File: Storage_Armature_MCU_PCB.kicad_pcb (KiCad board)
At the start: 4 copper layers, 163 x 152 mm, 221 parts, among them Q1 20N06, U10 NSI1200, U11 OPA333, U12 NSI1200, U13 OPA333, U14 USBLC6-2P6, U2 NSI1200, U23 RSCD06D3, U24 RSCD06D3, U25 RSCD06D3, U26 RSCD06D3, U3 NSI1200, U4 ADP3338AKCZ-3.3RL7, U5 ADP3338AKCZ-3.3RL7, U6 OPA333, U7 OPA333, U8 NSI1200, U9 OPA333

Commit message: VER1.0: добавил светодиоды, тестпоинты и мягкий старт 24В
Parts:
- added C100: 2.2u, Capacitor_SMD:C_0805_2012Metric_Pad1.18x1.45mm_HandSolder, B.Cu at (348.8, 111.8)
- added C101: 10n, Capacitor_SMD:C_0805_2012Metric_Pad1.18x1.45mm_HandSolder, B.Cu at (347.2, 115.2)
- added C102: 10n, Capacitor_SMD:C_0805_2012Metric_Pad1.18x1.45mm_HandSolder, B.Cu at (347.2, 108.0)
- added C103: 100n, Capacitor_SMD:C_0805_2012Metric_Pad1.18x1.45mm_HandSolder, B.Cu at (343.2, 111.8)
- added C104: 56p, Capacitor_SMD:C_0805_2012Metric_Pad1.18x1.45mm_HandSolder, B.Cu at (339.2, 111.8)
- added C72: 2.2u, Capacitor_SMD:C_0805_2012Metric_Pad1.18x1.45mm_HandSolder, B.Cu at (363.8, 157.8)
- added C75: 100n, Capacitor_SMD:C_0805_2012Metric_Pad1.18x1.45mm_HandSolder, B.Cu at (361.5, 157.8)
- added C76: 22n, Capacitor_SMD:C_0805_2012Metric_Pad1.18x1.45mm_HandSolder, F.Cu at (364.8, 157.8)
- added C77: 100n, Capacitor_SMD:C_0805_2012Metric_Pad1.18x1.45mm_HandSolder, B.Cu at (351.0, 157.8)
- added C78: 2.2u, Capacitor_SMD:C_0805_2012Metric_Pad1.18x1.45mm_HandSolder, B.Cu at (348.8, 157.8)
- added C79: 10n, Capacitor_SMD:C_0805_2012Metric_Pad1.18x1.45mm_HandSolder, B.Cu at (347.2, 161.2)
- added C80: 10n, Capacitor_SMD:C_0805_2012Metric_Pad1.18x1.45mm_HandSolder, B.Cu at (347.2, 154.0)
- added C81: 100n, Capacitor_SMD:C_0805_2012Metric_Pad1.18x1.45mm_HandSolder, B.Cu at (343.2, 157.8)
- added C86: 56p, Capacitor_SMD:C_0805_2012Metric_Pad1.18x1.45mm_HandSolder, B.Cu at (339.2, 157.8)
- added C87: 2.2u, Capacitor_SMD:C_0805_2012Metric_Pad1.18x1.45mm_HandSolder, B.Cu at (363.8, 134.8)
- added C88: 100n, Capacitor_SMD:C_0805_2012Metric_Pad1.18x1.45mm_HandSolder, B.Cu at (361.5, 134.8)
- added C89: 22n, Capacitor_SMD:C_0805_2012Metric_Pad1.18x1.45mm_HandSolder, F.Cu at (364.8, 134.8)
- added C90: 100n, Capacitor_SMD:C_0805_2012Metric_Pad1.18x1.45mm_HandSolder, B.Cu at (351.0, 134.8)
- added C91: 2.2u, Capacitor_SMD:C_0805_2012Metric_Pad1.18x1.45mm_HandSolder, B.Cu at (348.8, 134.8)
- added C92: 10n, Capacitor_SMD:C_0805_2012Metric_Pad1.18x1.45mm_HandSolder, B.Cu at (347.2, 138.2)
- added C93: 10n, Capacitor_SMD:C_0805_2012Metric_Pad1.18x1.45mm_HandSolder, B.Cu at (347.2, 131.0)
- added C94: 100n, Capacitor_SMD:C_0805_2012Metric_Pad1.18x1.45mm_HandSolder, B.Cu at (343.2, 134.8)
- added C95: 56p, Capacitor_SMD:C_0805_2012Metric_Pad1.18x1.45mm_HandSolder, B.Cu at (339.2, 134.8)
- added C96: 2.2u, Capacitor_SMD:C_0805_2012Metric_Pad1.18x1.45mm_HandSolder, B.Cu at (363.8, 111.8)
- added C97: 100n, Capacitor_SMD:C_0805_2012Metric_Pad1.18x1.45mm_HandSolder, B.Cu at (361.5, 111.8)
- added C98: 22n, Capacitor_SMD:C_0805_2012Metric_Pad1.18x1.45mm_HandSolder, F.Cu at (364.8, 111.8)
- added C99: 100n, Capacitor_SMD:C_0805_2012Metric_Pad1.18x1.45mm_HandSolder, B.Cu at (351.0, 111.8)
- added D13: ~, Package_TO_SOT_SMD:SOT-23, F.Cu at (339.1, 161.3)
- added D15: ~, Package_TO_SOT_SMD:SOT-23, F.Cu at (339.1, 138.3)
- added D16: ~, Package_TO_SOT_SMD:SOT-23, F.Cu at (339.1, 115.3)
- added D68: ~, LED_SMD:LED_0805_2012Metric, F.Cu at (237.8, 264.8)
- added D69: ~, LED_SMD:LED_0805_2012Metric, F.Cu at (262.8, 264.8)
- added D70: ~, LED_SMD:LED_0805_2012Metric, F.Cu at (287.8, 264.8)
- added D71: ~, LED_SMD:LED_0805_2012Metric, F.Cu at (312.8, 264.8)
- added J33: ~, Connector_Molex:Molex_Mini-Fit_Jr_5569-02A2_2x01_P4.20mm_Horizontal, F.Cu at (369.2, 149.2)
- added J36: ~, Connector_Molex:Molex_Mini-Fit_Jr_5569-02A2_2x01_P4.20mm_Horizontal, F.Cu at (369.2, 126.2)
- added J37: ~, Connector_Molex:Molex_Mini-Fit_Jr_5569-02A2_2x01_P4.20mm_Horizontal, F.Cu at (369.2, 103.2)
- added Q2: 20N06, Package_TO_SOT_SMD:TO-252-2, F.Cu at (230.2, 223.5)
- added R120: 1k, Resistor_SMD:R_0805_2012Metric_Pad1.20x1.40mm_HandSolder, F.Cu at (237.8, 267.5)
- added R121: 1k, Resistor_SMD:R_0805_2012Metric_Pad1.20x1.40mm_HandSolder, F.Cu at (262.8, 267.5)
- added R122: 1k, Resistor_SMD:R_0805_2012Metric_Pad1.20x1.40mm_HandSolder, F.Cu at (287.8, 267.5)
- added R123: 1k, Resistor_SMD:R_0805_2012Metric_Pad1.20x1.40mm_HandSolder, F.Cu at (312.8, 267.5)
- added R50: 10, Resistor_SMD:R_1206_3216Metric_Pad1.30x1.75mm_HandSolder, F.Cu at (370.8, 153.8)
- added R51: 100, Resistor_SMD:R_0805_2012Metric_Pad1.20x1.40mm_HandSolder, F.Cu at (368.0, 159.0)
- added R52: 100, Resistor_SMD:R_0805_2012Metric_Pad1.20x1.40mm_HandSolder, F.Cu at (368.0, 156.5)
- added R53: 10k, Resistor_SMD:R_0805_2012Metric_Pad1.20x1.40mm_HandSolder, F.Cu at (347.2, 159.0)
- added R56: 10k, Resistor_SMD:R_0805_2012Metric_Pad1.20x1.40mm_HandSolder, F.Cu at (347.2, 156.5)
- added R59: 20k, Resistor_SMD:R_0805_2012Metric_Pad1.20x1.40mm_HandSolder, F.Cu at (347.2, 161.2)
- added R60: 20k, Resistor_SMD:R_0805_2012Metric_Pad1.20x1.40mm_HandSolder, F.Cu at (347.2, 154.0)
- added R61: 120, Resistor_SMD:R_0805_2012Metric_Pad1.20x1.40mm_HandSolder, F.Cu at (339.2, 157.8)
- added R62: 10, Resistor_SMD:R_1206_3216Metric_Pad1.30x1.75mm_HandSolder, F.Cu at (370.8, 130.8)
- added R63: 100, Resistor_SMD:R_0805_2012Metric_Pad1.20x1.40mm_HandSolder, F.Cu at (368.0, 136.0)
- added R64: 100, Resistor_SMD:R_0805_2012Metric_Pad1.20x1.40mm_HandSolder, F.Cu at (368.0, 133.5)
- added R65: 10k, Resistor_SMD:R_0805_2012Metric_Pad1.20x1.40mm_HandSolder, F.Cu at (347.2, 136.0)
- added R66: 10k, Resistor_SMD:R_0805_2012Metric_Pad1.20x1.40mm_HandSolder, F.Cu at (347.2, 133.5)
- added R67: 20k, Resistor_SMD:R_0805_2012Metric_Pad1.20x1.40mm_HandSolder, F.Cu at (347.2, 138.2)
- added R68: 20k, Resistor_SMD:R_0805_2012Metric_Pad1.20x1.40mm_HandSolder, F.Cu at (347.2, 131.0)
- added R69: 120, Resistor_SMD:R_0805_2012Metric_Pad1.20x1.40mm_HandSolder, F.Cu at (339.2, 134.8)
- added R70: 10, Resistor_SMD:R_1206_3216Metric_Pad1.30x1.75mm_HandSolder, F.Cu at (370.8, 107.8)
- added R71: 100, Resistor_SMD:R_0805_2012Metric_Pad1.20x1.40mm_HandSolder, F.Cu at (368.0, 113.0)
- added R72: 100, Resistor_SMD:R_0805_2012Metric_Pad1.20x1.40mm_HandSolder, F.Cu at (368.0, 110.5)
- added R73: 10k, Resistor_SMD:R_0805_2012Metric_Pad1.20x1.40mm_HandSolder, F.Cu at (347.2, 113.0)
- added R74: 10k, Resistor_SMD:R_0805_2012Metric_Pad1.20x1.40mm_HandSolder, F.Cu at (347.2, 110.5)
- added R75: 20k, Resistor_SMD:R_0805_2012Metric_Pad1.20x1.40mm_HandSolder, F.Cu at (347.2, 115.2)
- added R76: 20k, Resistor_SMD:R_0805_2012Metric_Pad1.20x1.40mm_HandSolder, F.Cu at (347.2, 108.0)
- added R77: 120, Resistor_SMD:R_0805_2012Metric_Pad1.20x1.40mm_HandSolder, F.Cu at (339.2, 111.8)
- added R78: 470k, Resistor_SMD:R_0805_2012Metric_Pad1.20x1.40mm_HandSolder, F.Cu at (234.8, 232.5)
- added R79: 0, Resistor_SMD:R_1206_3216Metric_Pad1.30x1.75mm_HandSolder, F.Cu at (365.5, 268.8)
- added R80: 0, Resistor_SMD:R_1206_3216Metric_Pad1.30x1.75mm_HandSolder, F.Cu at (365.5, 245.8)
- added R81: 0, Resistor_SMD:R_1206_3216Metric_Pad1.30x1.75mm_HandSolder, F.Cu at (365.5, 222.8)
- added R82: 0, Resistor_SMD:R_1206_3216Metric_Pad1.30x1.75mm_HandSolder, F.Cu at (365.5, 199.8)
- added R83: 0, Resistor_SMD:R_1206_3216Metric_Pad1.30x1.75mm_HandSolder, F.Cu at (365.5, 176.8)
- added R84: 0, Resistor_SMD:R_1206_3216Metric_Pad1.30x1.75mm_HandSolder, F.Cu at (365.5, 153.8)
- added R85: 0, Resistor_SMD:R_1206_3216Metric_Pad1.30x1.75mm_HandSolder, F.Cu at (365.5, 130.8)
- added R86: 0, Resistor_SMD:R_1206_3216Metric_Pad1.30x1.75mm_HandSolder, F.Cu at (365.5, 107.8)
- added TP1: TestPoint, TestPoint:TestPoint_Loop_D1.80mm_Drill1.0mm_Beaded, F.Cu at (338.2, 270.2)
- added TP10: TestPoint, TestPoint:TestPoint_Loop_D1.80mm_Drill1.0mm_Beaded, F.Cu at (338.2, 243.5)
- added TP11: TestPoint, TestPoint:TestPoint_Loop_D1.80mm_Drill1.0mm_Beaded, F.Cu at (338.2, 220.5)
- added TP12: TestPoint, TestPoint:TestPoint_Loop_D1.80mm_Drill1.0mm_Beaded, F.Cu at (338.2, 197.5)
- added TP13: TestPoint, TestPoint:TestPoint_Loop_D1.80mm_Drill1.0mm_Beaded, F.Cu at (338.2, 174.5)
- added TP14: TestPoint, TestPoint:TestPoint_Loop_D1.80mm_Drill1.0mm_Beaded, F.Cu at (338.2, 151.5)
- added TP15: TestPoint, TestPoint:TestPoint_Loop_D1.80mm_Drill1.0mm_Beaded, F.Cu at (338.2, 128.5)
- added TP16: TestPoint, TestPoint:TestPoint_Loop_D1.80mm_Drill1.0mm_Beaded, F.Cu at (338.2, 105.5)
- added TP17: TestPoint, TestPoint:TestPoint_Loop_D1.80mm_Drill1.0mm_Beaded, F.Cu at (375.0, 268.8)
- added TP18: TestPoint, TestPoint:TestPoint_Loop_D1.80mm_Drill1.0mm_Beaded, F.Cu at (375.0, 245.8)
- added TP19: TestPoint, TestPoint:TestPoint_Loop_D1.80mm_Drill1.0mm_Beaded, F.Cu at (375.0, 222.8)
- added TP2: TestPoint, TestPoint:TestPoint_Loop_D1.80mm_Drill1.0mm_Beaded, F.Cu at (338.2, 247.2)
- added TP20: TestPoint, TestPoint:TestPoint_Loop_D1.80mm_Drill1.0mm_Beaded, F.Cu at (375.0, 199.8)
- added TP21: TestPoint, TestPoint:TestPoint_Loop_D1.80mm_Drill1.0mm_Beaded, F.Cu at (375.0, 176.8)
- added TP22: TestPoint, TestPoint:TestPoint_Loop_D1.80mm_Drill1.0mm_Beaded, F.Cu at (375.0, 153.8)
- added TP23: TestPoint, TestPoint:TestPoint_Loop_D1.80mm_Drill1.0mm_Beaded, F.Cu at (375.0, 130.8)
- added TP24: TestPoint, TestPoint:TestPoint_Loop_D1.80mm_Drill1.0mm_Beaded, F.Cu at (375.0, 107.8)
- added TP25: TestPoint, TestPoint:TestPoint_Loop_D1.80mm_Drill1.0mm_Beaded, F.Cu at (375.0, 272.5)
- added TP26: TestPoint, TestPoint:TestPoint_Loop_D1.80mm_Drill1.0mm_Beaded, F.Cu at (375.0, 249.5)
- added TP27: TestPoint, TestPoint:TestPoint_Loop_D1.80mm_Drill1.0mm_Beaded, F.Cu at (375.0, 226.5)
- added TP28: TestPoint, TestPoint:TestPoint_Loop_D1.80mm_Drill1.0mm_Beaded, F.Cu at (375.0, 203.5)
- added TP29: TestPoint, TestPoint:TestPoint_Loop_D1.80mm_Drill1.0mm_Beaded, F.Cu at (375.0, 180.5)
- added TP3: TestPoint, TestPoint:TestPoint_Loop_D1.80mm_Drill1.0mm_Beaded, F.Cu at (338.2, 224.2)
- added TP30: TestPoint, TestPoint:TestPoint_Loop_D1.80mm_Drill1.0mm_Beaded, F.Cu at (375.0, 157.5)
- added TP31: TestPoint, TestPoint:TestPoint_Loop_D1.80mm_Drill1.0mm_Beaded, F.Cu at (375.0, 134.5)
- added TP32: TestPoint, TestPoint:TestPoint_Loop_D1.80mm_Drill1.0mm_Beaded, F.Cu at (375.0, 111.5)
- added TP4: TestPoint, TestPoint:TestPoint_Loop_D1.80mm_Drill1.0mm_Beaded, F.Cu at (338.2, 201.2)
- added TP5: TestPoint, TestPoint:TestPoint_Loop_D1.80mm_Drill1.0mm_Beaded, F.Cu at (338.2, 178.2)
- added TP6: TestPoint, TestPoint:TestPoint_Loop_D1.80mm_Drill1.0mm_Beaded, F.Cu at (338.2, 155.2)
- added TP7: TestPoint, TestPoint:TestPoint_Loop_D1.80mm_Drill1.0mm_Beaded, F.Cu at (338.2, 132.2)
- added TP8: TestPoint, TestPoint:TestPoint_Loop_D1.80mm_Drill1.0mm_Beaded, F.Cu at (338.2, 109.2)
- added TP9: TestPoint, TestPoint:TestPoint_Loop_D1.80mm_Drill1.0mm_Beaded, F.Cu at (338.2, 266.5)
- added U15: NSI1200, Package_SO:SOIC-8_7.5x5.85mm_P1.27mm, F.Cu at (356.2, 157.8)
- added U16: OPA333, Package_TO_SOT_SMD:SOT-23-5, F.Cu at (343.2, 157.8)
- added U17: NSI1200, Package_SO:SOIC-8_7.5x5.85mm_P1.27mm, F.Cu at (356.2, 134.8)
- added U18: OPA333, Package_TO_SOT_SMD:SOT-23-5, F.Cu at (343.2, 134.8)
- added U19: NSI1200, Package_SO:SOIC-8_7.5x5.85mm_P1.27mm, F.Cu at (356.2, 111.8)
- added U20: OPA333, Package_TO_SOT_SMD:SOT-23-5, F.Cu at (343.2, 111.8)
- C82, C83, C84, C85: value 100n -> 10n
- R109, R112, R115, R118, R54: value 8.2k -> 4.7k
- moved R49 69.0 mm to (264.0, 90.0)
- moved H2 69.0 mm to (225.8, 92.5)
- moved H4 69.0 mm to (377.7, 92.5)
- moved D20 6.40 mm to (238.5, 231.5), turned to 0 degrees
- moved R55 5.83 mm to (228.0, 232.5), turned to -90 degrees
- moved C70 4.85 mm to (231.5, 231.5), turned to 0 degrees
- moved C82 3.48 mm to (243.5, 271.2), turned to 90 degrees
- moved C83 3.48 mm to (268.5, 271.2), turned to 90 degrees
- moved C84 3.48 mm to (293.5, 271.2), turned to 90 degrees
- moved C85 3.48 mm to (318.5, 271.2), turned to 90 degrees
- moved R108 2.25 mm to (248.0, 271.2)
- moved R110 2.25 mm to (245.8, 271.2)
- moved R113 2.25 mm to (270.8, 271.2)
- moved R116 2.25 mm to (295.8, 271.2)
- moved R119 2.25 mm to (320.8, 271.2)
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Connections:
- C70 pad 2: GNDD -> Net-(D20-A)
- C82 pad 1: /Solenoid_control_1/Coil_1_CTRL -> Net-(Q10-G)
- C83 pad 1: /Solenoid_control_2/Coil_1_CTRL -> Net-(Q11-G)
- C84 pad 1: /Solenoid_control_3/Coil_1_CTRL -> Net-(Q12-G)
- C85 pad 1: /Solenoid_control_4/Coil_1_CTRL -> Net-(Q13-G)
- D20 pad 2: GNDD -> Net-(D20-A)
- D56 pad 3: /Solenoid_control_1/Coil_1_CTRL -> /Solenoid1_MCU
- D59 pad 3: /Solenoid_control_2/Coil_1_CTRL -> /Solenoid2_MCU
- D62 pad 3: /Solenoid_control_3/Coil_1_CTRL -> /Solenoid3_MCU
- D65 pad 3: /Solenoid_control_4/Coil_1_CTRL -> /Solenoid4_MCU
- Q1 pad 3: GNDD -> Net-(D20-A)
- R108 pad 1: /Solenoid_control_1/Coil_1_CTRL -> /Solenoid1_MCU
- R111 pad 1: /Solenoid_control_2/Coil_1_CTRL -> /Solenoid2_MCU
- R114 pad 1: /Solenoid_control_3/Coil_1_CTRL -> /Solenoid3_MCU
- R117 pad 1: /Solenoid_control_4/Coil_1_CTRL -> /Solenoid4_MCU
- R13 pad 1: GNDD -> Net-(R13-Pad1)
- R18 pad 2: GNDD -> Net-(R18-Pad2)
- R20 pad 1: GNDD -> Net-(R18-Pad2)
- R28 pad 2: GNDD -> Net-(R28-Pad2)
- R3 pad 2: GNDD -> Net-(R3-Pad2)
- R30 pad 1: GNDD -> Net-(R28-Pad2)
- R36 pad 2: GNDD -> Net-(R36-Pad2)
- R4 pad 2: GNDD -> Net-(R13-Pad1)
- R41 pad 1: GNDD -> Net-(R36-Pad2)
- R7 pad 1: GNDD -> Net-(R3-Pad2)
- U1 pad 10: unconnected-(U1-PC2-Pad10) -> /Sensor_3/P_measure_MCU
- U1 pad 11: unconnected-(U1-PC3-Pad11) -> /Sensor_4/P_measure_MCU
- U1 pad 15: unconnected-(U1-PA1-Pad15) -> /Sensor_5/P_measure_MCU
- U1 pad 16: unconnected-(U1-PA2-Pad16) -> /Sensor_6/P_measure_MCU
- U1 pad 17: unconnected-(U1-PA3-Pad17) -> /Sensor_7/P_measure_MCU
- U1 pad 20: unconnected-(U1-PA4-Pad20) -> /Sensor_8/P_measure_MCU
- U1 pad 50: unconnected-(U1-PA15-Pad50) -> /Solenoid1_MCU
- U1 pad 51: unconnected-(U1-PC10-Pad51) -> /Solenoid2_MCU
- U1 pad 52: unconnected-(U1-PC11-Pad52) -> /Solenoid3_MCU
- U1 pad 53: unconnected-(U1-PC12-Pad53) -> /Solenoid4_MCU
- U1 pad 8: unconnected-(U1-PC0-Pad8) -> /Sensor_1/P_measure_MCU
- U1 pad 9: unconnected-(U1-PC1-Pad9) -> /Sensor_2/P_measure_MCU
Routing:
- net /Sensor_8/P_measure_MCU: track 0.00 -> 135.4 mm, vias 0 -> 1
- net /Sensor_7/P_measure_MCU: track 0.00 -> 111.0 mm, vias 0 -> 1
- net /Solenoid1_MCU: track 0.00 -> 92.1 mm
- net /Sensor_6/P_measure_MCU: track 0.00 -> 86.6 mm, vias 0 -> 1
- net /Sensor_1/P_measure_MCU: track 6.12 -> 88.2 mm
- net /Solenoid2_MCU: track 0.00 -> 63.2 mm
- net /Sensor_2/P_measure_MCU: track 6.12 -> 66.7 mm
- net /Sensor_5/P_measure_MCU: track 6.12 -> 64.0 mm
- net /Solenoid4_MCU: track 0.00 -> 46.5 mm
- net /Solenoid3_MCU: track 0.00 -> 45.8 mm
- net /Sensor_3/P_measure_MCU: track 6.12 -> 50.4 mm
- net /Sensor_4/P_measure_MCU: track 6.12 -> 43.1 mm
- net GND: track 89.1 -> 115.3 mm, vias 87 -> 106
- net +3.3V: track 78.9 -> 103.2 mm, vias 46 -> 55
- net /CANH: track 39.2 -> 17.2 mm
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- added copper zone on B.Cu, net /CANH
- added copper zone on F.Cu, net /CANL
- added copper zone on In2.Cu, net GNDD
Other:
- board size 163 x 152 mm -> 163 x 221 mm
- board text added: "GNDD"
- board text added: "Signal"

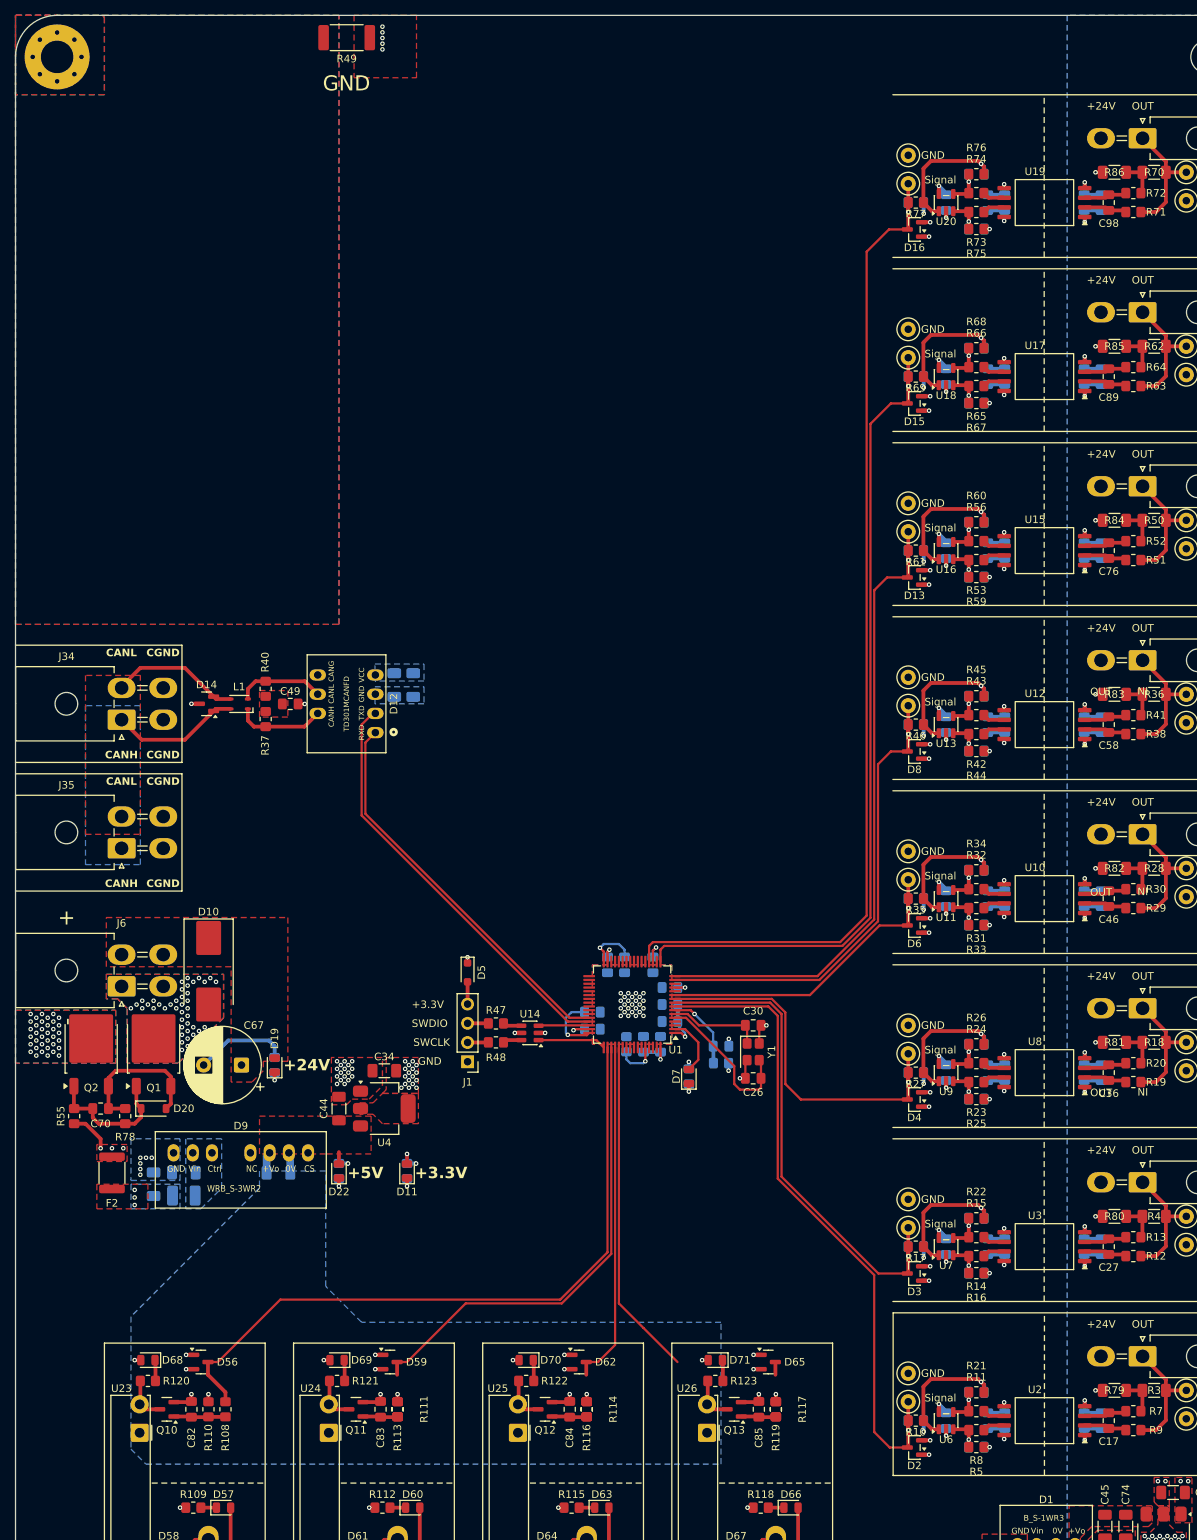
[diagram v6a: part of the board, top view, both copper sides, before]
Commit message: VER1.0: добавил RS485, Board ID, вырезы в плате
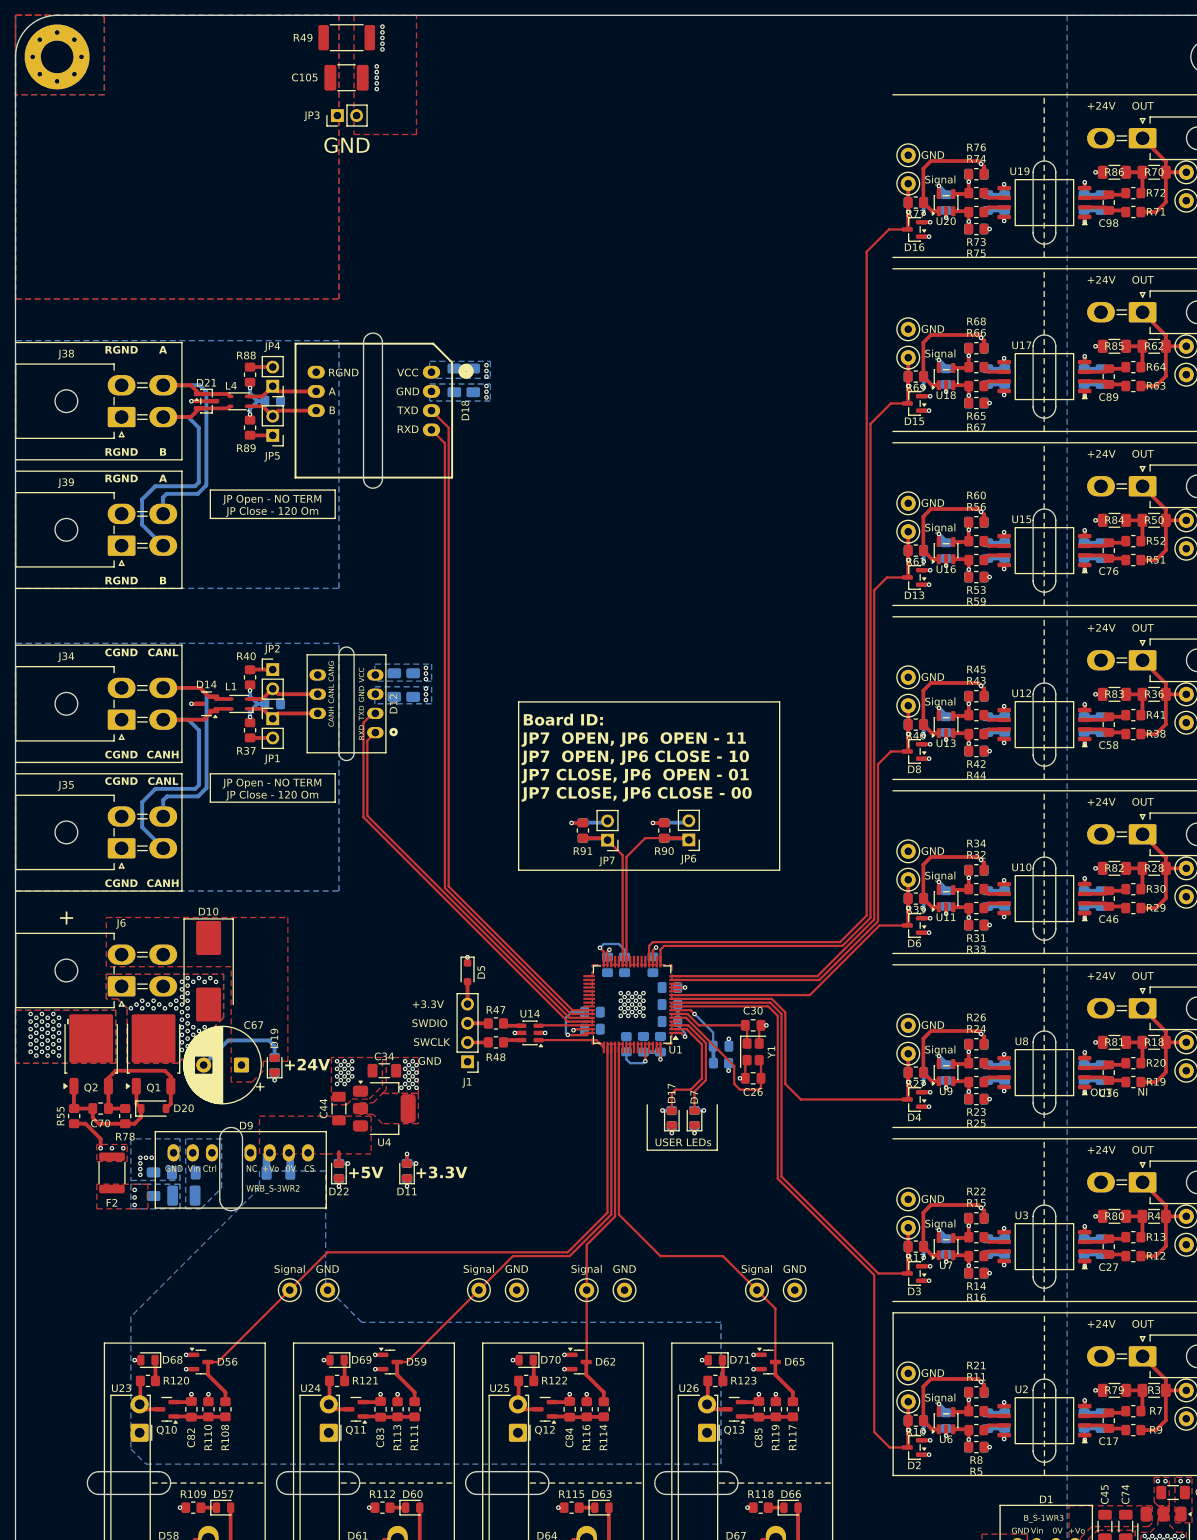
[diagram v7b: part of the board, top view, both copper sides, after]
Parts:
- added C105: 2.2n, Capacitor_SMD:C_1812_4532Metric_Pad1.57x3.40mm_HandSolder, F.Cu at (264.0, 95.2)
- added C106: 10n, Capacitor_SMD:C_0805_2012Metric_Pad1.18x1.45mm_HandSolder, B.Cu at (254.2, 138.0)
- added C107: 10u, Capacitor_SMD:C_1206_3216Metric_Pad1.33x1.80mm_HandSolder, B.Cu at (280.8, 135.2)
- added C108: 100n, Capacitor_SMD:C_1206_3216Metric_Pad1.33x1.80mm_HandSolder, B.Cu at (278.2, 135.2)
- added C109: 100n, Capacitor_SMD:C_0805_2012Metric_Pad1.18x1.45mm_HandSolder, B.Cu at (306.0, 194.8)
- added C110: 100n, Capacitor_SMD:C_0805_2012Metric_Pad1.18x1.45mm_HandSolder, B.Cu at (295.2, 194.8)
- added D17: ~, LED_SMD:LED_0805_2012Metric, F.Cu at (307.0, 232.8)
- added D18: TD301D485H-A, MORNSUN:TD301D485H-AB, F.Cu at (267.6, 139.2)
- added D21: ~, Package_TO_SOT_SMD:SOT-23, F.Cu at (245.5, 138.0)
- added J38: ~, Connector_Molex:Molex_Mini-Fit_Jr_5569-04A2_2x02_P4.20mm_Horizontal, F.Cu at (234.3, 140.1)
- added J39: ~, Connector_Molex:Molex_Mini-Fit_Jr_5569-04A2_2x02_P4.20mm_Horizontal, F.Cu at (234.3, 157.1)
- added JP1: Jumper_2_Small_Bridged, Connector_PinHeader_2.54mm:PinHeader_1x02_P2.54mm_Vertical, F.Cu at (254.2, 180.0)
- added JP2: Jumper_2_Small_Bridged, Connector_PinHeader_2.54mm:PinHeader_1x02_P2.54mm_Vertical, F.Cu at (254.2, 173.5)
- added JP3: Jumper_2_Small_Bridged, Connector_PinHeader_2.54mm:PinHeader_1x02_P2.54mm_Vertical, F.Cu at (262.8, 100.2)
- added JP4: Jumper_2_Small_Bridged, Connector_PinHeader_2.54mm:PinHeader_1x02_P2.54mm_Vertical, F.Cu at (254.2, 136.0)
- added JP5: Jumper_2_Small_Bridged, Connector_PinHeader_2.54mm:PinHeader_1x02_P2.54mm_Vertical, F.Cu at (254.2, 142.5)
- added JP6: Jumper_2_Small_Bridged, Connector_PinHeader_2.54mm:PinHeader_1x02_P2.54mm_Vertical, F.Cu at (309.2, 196.0)
- added JP7: Jumper_2_Small_Bridged, Connector_PinHeader_2.54mm:PinHeader_1x02_P2.54mm_Vertical, F.Cu at (298.5, 196.0)
- added L4: ~, Inductor_SMD:L_CommonModeChoke_TDK_ACM2520-2P, F.Cu at (249.8, 138.0)
- added R87: 1k, Resistor_SMD:R_0805_2012Metric_Pad1.20x1.40mm_HandSolder, B.Cu at (307.0, 232.8)
- added R88: 59, Resistor_SMD:R_0805_2012Metric_Pad1.20x1.40mm_HandSolder, F.Cu at (251.2, 134.5)
- added R89: 59, Resistor_SMD:R_0805_2012Metric_Pad1.20x1.40mm_HandSolder, F.Cu at (251.2, 141.5)
- added R90: 10k, Resistor_SMD:R_0805_2012Metric_Pad1.20x1.40mm_HandSolder, F.Cu at (306.0, 194.8)
- added R91: 10k, Resistor_SMD:R_0805_2012Metric_Pad1.20x1.40mm_HandSolder, F.Cu at (295.2, 194.8)
- added TP36: TestPoint, TestPoint:TestPoint_Loop_D1.80mm_Drill1.0mm_Beaded, F.Cu at (300.8, 255.5)
- added TP37: TestPoint, TestPoint:TestPoint_Loop_D1.80mm_Drill1.0mm_Beaded, F.Cu at (261.5, 255.5)
- added TP38: TestPoint, TestPoint:TestPoint_Loop_D1.80mm_Drill1.0mm_Beaded, F.Cu at (286.5, 255.5)
- added TP39: TestPoint, TestPoint:TestPoint_Loop_D1.80mm_Drill1.0mm_Beaded, F.Cu at (323.2, 255.5)
- added TP40: TestPoint, TestPoint:TestPoint_Loop_D1.80mm_Drill1.0mm_Beaded, F.Cu at (256.5, 255.5)
- added TP41: TestPoint, TestPoint:TestPoint_Loop_D1.80mm_Drill1.0mm_Beaded, F.Cu at (281.5, 255.5)
- added TP42: TestPoint, TestPoint:TestPoint_Loop_D1.80mm_Drill1.0mm_Beaded, F.Cu at (295.8, 255.5)
- added TP43: TestPoint, TestPoint:TestPoint_Loop_D1.80mm_Drill1.0mm_Beaded, F.Cu at (318.2, 255.5)
- C49: moved to B.Cu
- R49: value 0 -> 1M
- moved D7 5.55 mm to (310.0, 232.8)
- moved R6 5.55 mm to (310.0, 232.8)
- moved R40 2.56 mm to (251.2, 174.5)
- moved R37 2.54 mm to (251.2, 181.5)
- moved C49 2.31 mm to (254.2, 178.0)
- moved R111 2.25 mm to (273.0, 271.2)
- moved R114 2.25 mm to (298.0, 271.2)
- moved R117 2.25 mm to (323.0, 271.2)
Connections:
- J34 pad 1: /CANH -> GND_CAN
- J34 pad 2: /CANL -> GND_CAN
- J34 pad 3: GND_CAN -> /CANH
- J34 pad 4: GND_CAN -> /CANL
- J35 pad 1: /CANH -> GND_CAN
- J35 pad 2: /CANL -> GND_CAN
- J35 pad 3: GND_CAN -> /CANH
- J35 pad 4: GND_CAN -> /CANL
- R37 pad 2: Net-(D12-CANH) -> Net-(JP1-B)
- R40 pad 1: Net-(D12-CANL) -> Net-(JP2-A)
- U1 pad 2: Net-(D7-A) -> Net-(D17-A)
- U1 pad 26: unconnected-(U1-PB0-Pad26) -> Net-(JP6-A)
- U1 pad 27: unconnected-(U1-PB1-Pad27) -> Net-(JP7-A)
- U1 pad 3: unconnected-(U1-PC14-Pad3) -> Net-(D7-A)
- U1 pad 42: unconnected-(U1-PA9-Pad42) -> /RS_TXD_MCU
- U1 pad 43: unconnected-(U1-PA10-Pad43) -> /RS_RXD_MCU
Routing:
- net /RS_TXD_MCU: track 0.00 -> 89.2 mm
- net /RS_RXD_MCU: track 0.00 -> 87.3 mm
- net /B: track 0.00 -> 37.7 mm
- net /A: track 0.00 -> 36.5 mm
- net Net-(JP6-A): track 0.00 -> 26.6 mm
- net Net-(JP7-A): track 0.00 -> 24.1 mm
- net /CANH: track 17.2 -> 37.7 mm
- net /CANL: track 18.3 -> 36.5 mm
- net Net-(D17-A): track 0.00 -> 16.0 mm
- net /Solenoid4_MCU: track 46.5 -> 61.2 mm
- net Net-(D18-B): track 0.00 -> 9.88 mm
- net Net-(D18-A): track 0.00 -> 9.87 mm
- net GND: track 115.3 -> 123.6 mm, vias 106 -> 118
- net Net-(C49-Pad1): track 0.00 -> 6.79 mm, vias 0 -> 2
- net Net-(C106-Pad1): track 0.00 -> 6.79 mm, vias 0 -> 2
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- added copper zone on B.Cu, net GND_CAN
- added copper zone on In2.Cu, net GND_CAN
- added copper zone on B.Cu, net GND_RS485
- added copper zone on In1.Cu, net GND_RS485
- added copper zone on In2.Cu, net GND_RS485
- removed copper zone on B.Cu, net /CANH
- removed copper zone on F.Cu, net /CANL
- removed copper zone on F.Cu, net Net-(C49-Pad1)
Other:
- outline, holes or cut-outs redrawn
- board text added: "A"
- board text added: "B"
- board text added: "Board ID: JP7 OPEN, JP6 OPEN - 11 JP7 OPEN, JP6 CLOSE - 10 JP7 CLOSE, JP6 OPEN - 01 JP7 CLOSE, JP6 CLOSE - 00"
- board text added: "JP Open - NO TERM JP Close - 120 Om"
- board text added: "RGND"
- board text added: "USER LEDs"
